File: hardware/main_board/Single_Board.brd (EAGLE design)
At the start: 49.9 x 49.5 mm, 54 parts, among them J2 U.FL, J3 AVR_SPI_PROG_3X2NS, Q1 2N7002, Q2 AO3400A, Q3 S9015, U1 INA199B1DCKR, U2 MCP1703T-3302E/CB, U4 W25X40CLUXIG_TR, U5 ATMEGA328PB-AU, X1 32.768KHZ-FC-135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

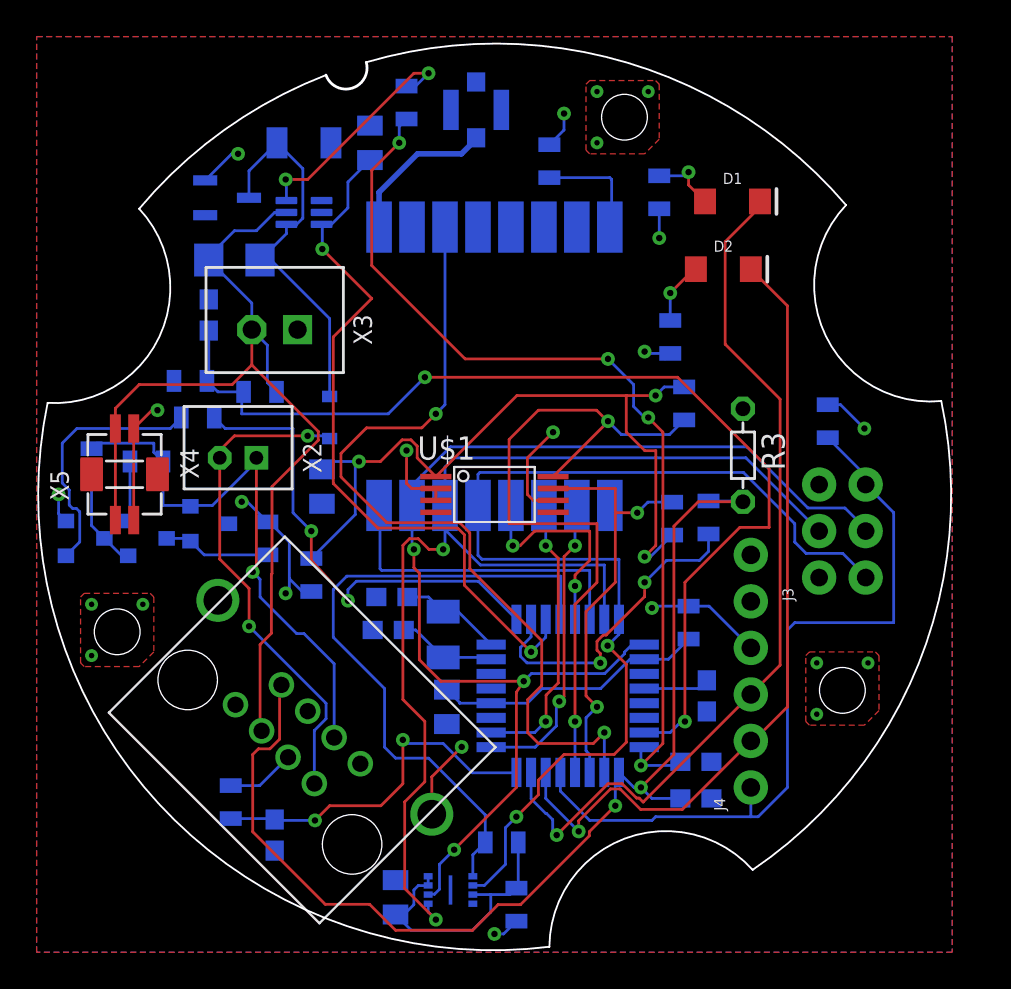
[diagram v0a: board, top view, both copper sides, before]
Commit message: Board improvements: Fixed 8P8C jack footprint. Better antenna trace impedance. Added anti-static resistor to antenna
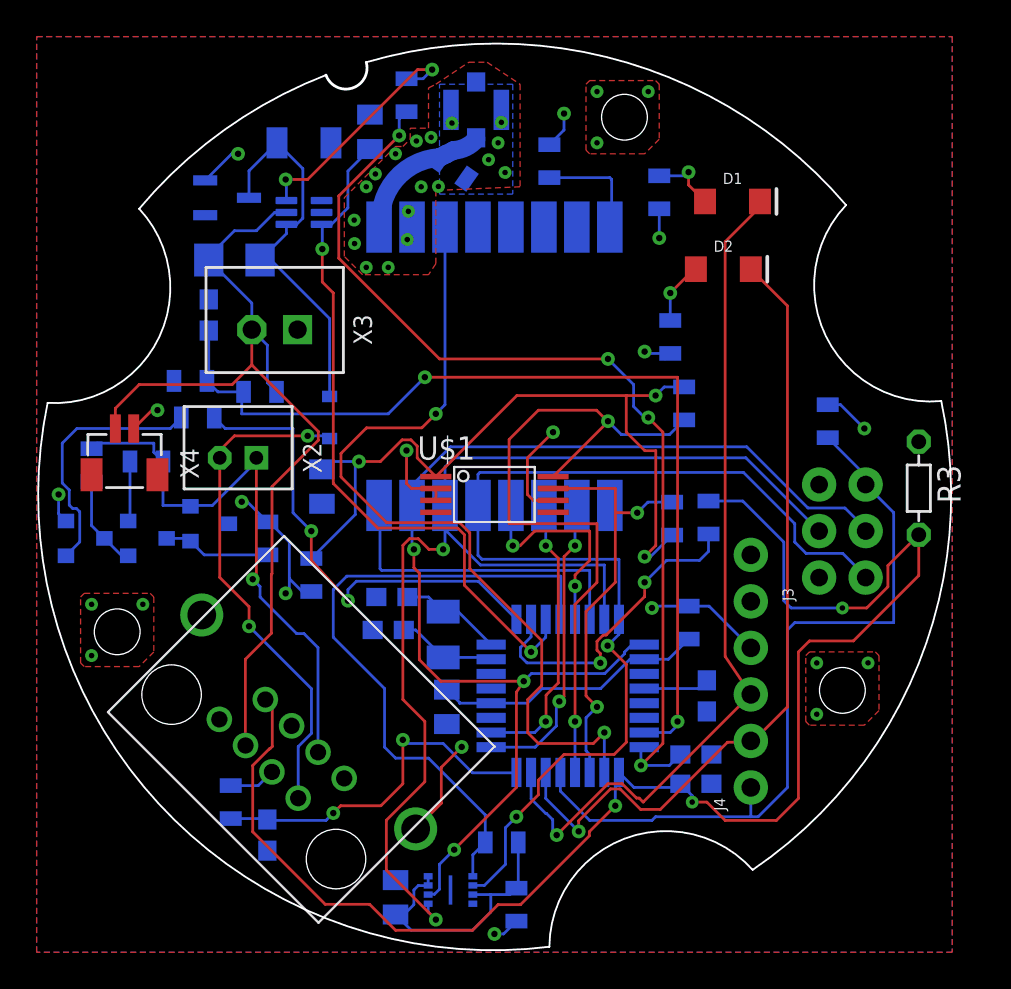
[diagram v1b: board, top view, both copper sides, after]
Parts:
- removed X5: BM02B-SRSS-TB, main_board:BM02B-SRSS-TB
- added R22: 10k, SparkFun-Resistors:0805
- moved R3 9.77 mm to (48.2, 25.3)
- moved U$3 1.19 mm to (13.6, 11.3)
- moved C4 0.80 mm to (36.0, 9.20)
- moved C9 0.60 mm to (18.2, 44.8)
- moved C2 0.40 mm to (12.6, 6.40)
- moved C8 0.40 mm to (36.0, 10.8)
- moved R18 0.40 mm to (20.2, 46.8)
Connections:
- net ANT: now also R22.2
- net BATT_+VE: no longer X5.1
- net GND: now also R22.1; no longer X5.2
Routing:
- net TEMP_SENSE: track 61.0 -> 83.0 mm, vias 2 -> 3
- net BATT_SENSE: track 57.1 -> 51.9 mm
- net BATT_+VE: track 53.5 -> 49.6 mm
- net GND: track 20.7 -> 16.9 mm, vias 13 -> 31
- net CUR_SENSE: track 51.2 -> 54.0 mm
- net TX: track 48.2 -> 46.8 mm
- net ANT: track 8.48 -> 9.80 mm
- net N$16: track 3.77 -> 2.56 mm
- net CUR_SENSE_PWR: track 39.4 -> 38.3 mm
- net MOSI: track 66.4 -> 67.2 mm
- net SOLAR_NEG: track 30.9 -> 31.5 mm
- net VSOLAR: track 27.3 -> 27.8 mm
